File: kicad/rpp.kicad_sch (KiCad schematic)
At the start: 13 parts, among them J1 SolderPad, J2 SolderPad, J3 SolderPad, J4 SolderPad, Q1 CSD19537Q3, U1 LM5050-1

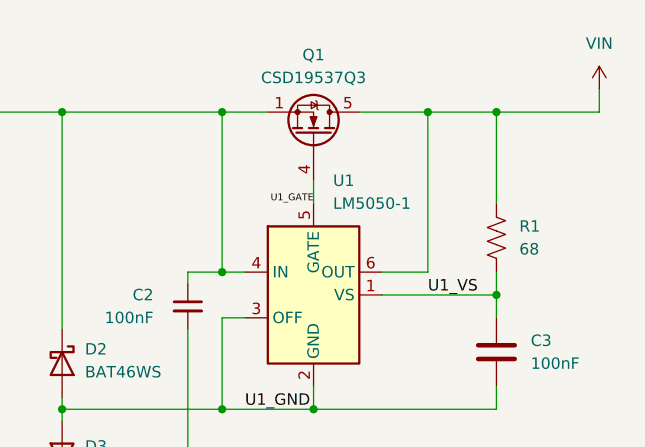
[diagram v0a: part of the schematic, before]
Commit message: Wrong design files initially commited
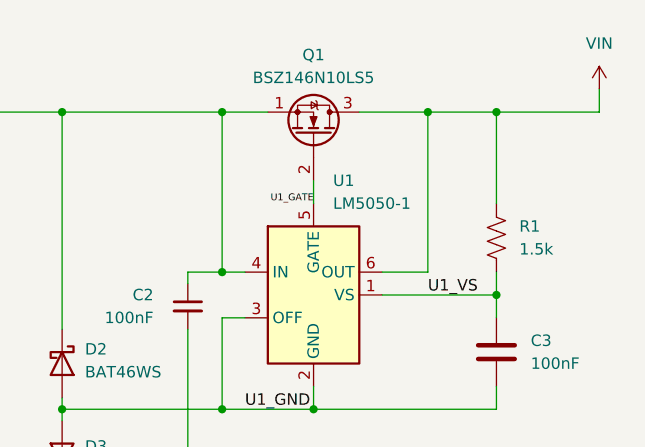
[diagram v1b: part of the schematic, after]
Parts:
- Q1: value CSD19537Q3 -> BSZ146N10LS5; footprint Package_SON_JJ:Texas_DQG0008A_3.3x3.3mm_P0.65mm_ThermalVias-D0.3mm -> Package_SON_JJ:Infineon_PG-TSDSON-8-26_3.3x3.3mm_P0.65mm_ThermalVias-D0.3mm; symbol Transistor_FET:CSD19537Q3 -> Julian_Symbols:BSZ096N10LS5; FT Rotation Offset 0 -> -90; LCSC PN C134143 -> C3289340; Manufacturer Texas Instruments -> Infineon Technologies; Part Number CSD19537Q3T -> BSZ146N10LS5ATMA1
- R1: value 68 -> 1.5k; LCSC PN C27592 -> C22843; Part Number 0603WAF680JT5E -> 0603WAF1501T5E; Part Type Preferred Extended -> Basic
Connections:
- net U1_GATE: now also Q1.2 (G); no longer Q1.4 (G)
- net VBAT: no longer Q1.2 (S), Q1.3 (S)
- net VIN: now also Q1.3 (D); no longer Q1.5 (D)
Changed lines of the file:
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@@
 	(title_block
 		(title "Super Step Down V3")
-		(date "2025-12-02")
+		(date "2026-02-06")
 		(rev "D")
 		(company "Author: Julian Joaquin")
 		(comment 1 "Licensed under CERN-OHL-W version 2")
-		(comment 2 "Copyright © Julian Joaquin, 2025")
+		(comment 2 "Copyright © Julian Joaquin, 2026")
 		(comment 4 "A 12S battery eliminator circuit (BEC) for UAS applications.")
 	)
@@
 		(dnp no)
 		(fields_autoplaced yes)
-		(property "Reference" "#PWR08"
+		(property "Reference" "#PWR04"
 			(at 130.81 88.9 0)
 			(effects
@@
 			(project "SSDV3"
 				(path "/ea689c3b-fea3-4fc0-9d65-1fb672b240d8/2c5420f9-cdfd-4ae0-879c-cf9dbf3cb514"
-					(reference "#PWR08")
+					(reference "#PWR04")
 					(unit 1)
 				)
@@
 		(dnp no)
 		(fields_autoplaced yes)
-		(property "Reference" "#PWR023"
+		(property "Reference" "#PWR06"
 			(at 172.72 168.91 0)
 			(effects
@@
 			(project "SSDV3"
 				(path "/ea689c3b-fea3-4fc0-9d65-1fb672b240d8/2c5420f9-cdfd-4ae0-879c-cf9dbf3cb514"
-					(reference "#PWR023")
+					(reference "#PWR06")
 					(unit 1)
 				)
@@
 		(on_board yes)
 		(dnp no)
-		(property "Reference" "#PWR09"
+		(property "Reference" "#PWR05"
 			(at 143.51 80.01 0)
 			(effects
@@
 			(project "SSDV3"
 				(path "/ea689c3b-fea3-4fc0-9d65-1fb672b240d8/2c5420f9-cdfd-4ae0-879c-cf9dbf3cb514"
-					(reference "#PWR09")
+					(reference "#PWR05")
 					(unit 1)
 				)
@@
 		(dnp no)
 		(fields_autoplaced yes)
-		(property "Reference" "#FLG06"
+		(property "Reference" "#FLG01"
 			(at 159.385 168.91 0)
 			(effects
@@
 			(project "SSDV3"
 				(path "/ea689c3b-fea3-4fc0-9d65-1fb672b240d8/2c5420f9-cdfd-4ae0-879c-cf9dbf3cb514"
-					(reference "#FLG06")
+					(reference "#FLG01")
 					(unit 1)
 				)
@@
 		(on_board yes)
 		(dnp no)
-		(property "Reference" "#PWR014"
+		(property "Reference" "#PWR09"
 			(at 215.9 130.81 0)
 			(effects
@@
 			(project "SSDV3"
 				(path "/ea689c3b-fea3-4fc0-9d65-1fb672b240d8/2c5420f9-cdfd-4ae0-879c-cf9dbf3cb514"
-					(reference "#PWR014")
+					(reference "#PWR09")
 					(unit 1)
 				)
@@
 		(on_board yes)
 		(dnp no)
-		(property "Reference" "#PWR018"
+		(property "Reference" "#PWR07"
 			(at 162.56 173.99 0)
 			(effects
@@
 			(project "SSDV3"
 				(path "/ea689c3b-fea3-4fc0-9d65-1fb672b240d8/2c5420f9-cdfd-4ae0-879c-cf9dbf3cb514"
-					(reference "#PWR018")
-					(unit 1)
-				)
-			)
-		)
-	)
-	(symbol
-		(lib_id "power:PWR_FLAG")
-		(at 161.29 179.07 90)
-		(unit 1)
-		(exclude_from_sim no)
-		(in_bom yes)
-		(on_board yes)
-		(dnp no)
-		(fields_autoplaced yes)
-		(property "Reference" "#FLG08"
-			(at 159.385 179.07 0)
-			(effects
-				(font
-					(size 1.27 1.27)
-				)
-				(hide yes)
-			)
-		)
-		(property "Value" "PWR_FLAG"
-			(at 157.48 179.07 90)
-			(effects
-				(font
-					(size 1.27 1.27)
-				)
-				(justify left)
-			)
-		)
-		(property "Footprint" ""
-			(at 161.29 179.07 0)
-			(effects
-				(font
-					(size 1.27 1.27)
-				)
-				(hide yes)
-			)
-		)
-		(property "Datasheet" "~"
-			(at 161.29 179.07 0)
-			(effects
-				(font
-					(size 1.27 1.27)
-				)
-				(hide yes)
-			)
-		)
-		(property "Description" "Special symbol for telling ERC where power comes from"
-			(at 161.29 179.07 0)
-			(effects
-				(font
-					(size 1.27 1.27)
-				)
-				(hide yes)
-			)
-		)
-		(pin "1"
-		)
-		(instances
-			(project "SSDV3"
-				(path "/ea689c3b-fea3-4fc0-9d65-1fb672b240d8/2c5420f9-cdfd-4ae0-879c-cf9dbf3cb514"
-					(reference "#FLG08")
+					(reference "#PWR07")
 					(unit 1)
 				)
@@
 			)
 		)
-		(property "Value" "68"
+		(property "Value" "1.5k"
 			(at 207.01 93.98 0)
 			(effects
@@
 			)
 		)
-		(property "Description" "RES 68Ω 1% 75V 100mW 0603"
+		(property "Description" "RES 1.5kΩ 1% 75V 100mW 0603"
 			(at 204.47 92.71 0)
 			(effects
@@
 			)
 		)
-		(property "LCSC PN" "C27592"
+		(property "LCSC PN" "C22843"
 			(at 204.47 92.71 0)
 			(effects
@@
 			)
 		)
-		(property "Part Type" "Preferred Extended"
+		(property "Part Type" "Basic"
 			(at 204.47 92.71 0)
 			(effects
@@
 			)
 		)
-		(property "Part Number" "0603WAF680JT5E"
+		(property "Part Number" "0603WAF1501T5E"
 			(at 204.47 92.71 0)
 			(effects
@@
 				(path "/ea689c3b-fea3-4fc0-9d65-1fb672b240d8/2c5420f9-cdfd-4ae0-879c-cf9dbf3cb514"
 					(reference "R1")
+					(unit 1)
+				)
+			)
+		)
+	)
+	(symbol
+		(lib_id "power:PWR_FLAG")
+		(at 161.29 179.07 90)
+		(unit 1)
+		(exclude_from_sim no)
+		(in_bom yes)
+		(on_board yes)
+		(dnp no)
+		(fields_autoplaced yes)
+		(property "Reference" "#FLG03"
+			(at 159.385 179.07 0)
+			(effects
+				(font
+					(size 1.27 1.27)
+				)
+				(hide yes)
+			)
+		)
+		(property "Value" "PWR_FLAG"
+			(at 157.48 179.07 90)
+			(effects
+				(font
+					(size 1.27 1.27)
+				)
+				(justify left)
+			)
+		)
+		(property "Footprint" ""
+			(at 161.29 179.07 0)
+			(effects
+				(font
+					(size 1.27 1.27)
+				)
+				(hide yes)
+			)
+		)
+		(property "Datasheet" "~"
+			(at 161.29 179.07 0)
+			(effects
+				(font
+					(size 1.27 1.27)
+				)
+				(hide yes)
+			)
+		)
+		(property "Description" "Special symbol for telling ERC where power comes from"
+			(at 161.29 179.07 0)
+			(effects
+				(font
+					(size 1.27 1.27)
+				)
+				(hide yes)
+			)
+		)
+		(pin "1"
+		)
+		(instances
+			(project "SSDV3"
+				(path "/ea689c3b-fea3-4fc0-9d65-1fb672b240d8/2c5420f9-cdfd-4ae0-879c-cf9dbf3cb514"
+					(reference "#FLG03")
 					(unit 1)
 				)
@@
 	)
 	(symbol
-		(lib_id "Transistor_FET:CSD19537Q3")
+		(lib_id "Julian_Symbols:BSZ096N10LS5")
 		(at 184.15 81.28 270)
 		(mirror x)
@@
 			)
 		)
-		(property "Value" "CSD19537Q3"
+		(property "Value" "BSZ146N10LS5"
 			(at 184.15 74.93 90)
 			(effects
@@
 			)
 		)
-		(property "Footprint" "Package_SON_JJ:Texas_DQG0008A_3.3x3.3mm_P0.65mm_ThermalVias-D0.3mm"
+		(property "Footprint" "Package_SON_JJ:Infineon_PG-TSDSON-8-26_3.3x3.3mm_P0.65mm_ThermalVias-D0.3mm"
 			(at 182.245 76.2 0)
 			(effects
@@
 			)
 		)
-		(property "Datasheet" "http://www.ti.com/lit/ds/symlink/csd19537q3.pdf"
+		(property "Datasheet" "https://www.infineon.com/assets/row/public/documents/24/49/infineon-bsz146n10ls5-datasheet-en.pdf"
 			(at 180.34 76.2 0)
 			(effects
@@
 			)
 		)
-		(property "Description" "MOSFET N-CH 100V 53A VSON-8(3.3x3.3)"
+		(property "Description" "MOSFET N-CH 100V 44A TSDSON-8FL"
 			(at 184.15 81.28 0)
 			(effects
@@
 			)
 		)
-		(property "LCSC PN" "C134143"
+		(property "LCSC PN" "C3289340"
 			(at 184.15 81.28 90)
 			(effects
@@
 			)
 		)
-		(property "Manufacturer" "Texas Instruments"
+		(property "Manufacturer" "Infineon Technologies"
 			(at 184.15 81.28 90)
 			(effects
@@
 			)
 		)
-		(property "Part Number" "CSD19537Q3T"
+		(property "Part Number" "BSZ146N10LS5ATMA1"
 			(at 184.15 81.28 90)
 			(effects
@@
 			)
 		)
-		(property "FT Rotation Offset" "0"
+		(property "FT Rotation Offset" "-90"
 			(at 184.15 81.28 90)
 			(effects
@@
 			)
 		)
-		(pin "5"
-		)
 		(pin "2"
 		)
@@
 		)
 		(pin "1"
-		)
-		(pin "4"
 		)
 		(instances
@@
 		(dnp no)
 		(fields_autoplaced yes)
-		(property "Reference" "#PWR013"
+		(property "Reference" "#PWR08"
 			(at 215.9 80.01 0)
 			(effects
@@
 			(project "SSDV3"
 				(path "/ea689c3b-fea3-4fc0-9d65-1fb672b240d8/2c5420f9-cdfd-4ae0-879c-cf9dbf3cb514"
-					(reference "#PWR013")
+					(reference "#PWR08")
 					(unit 1)
 				)

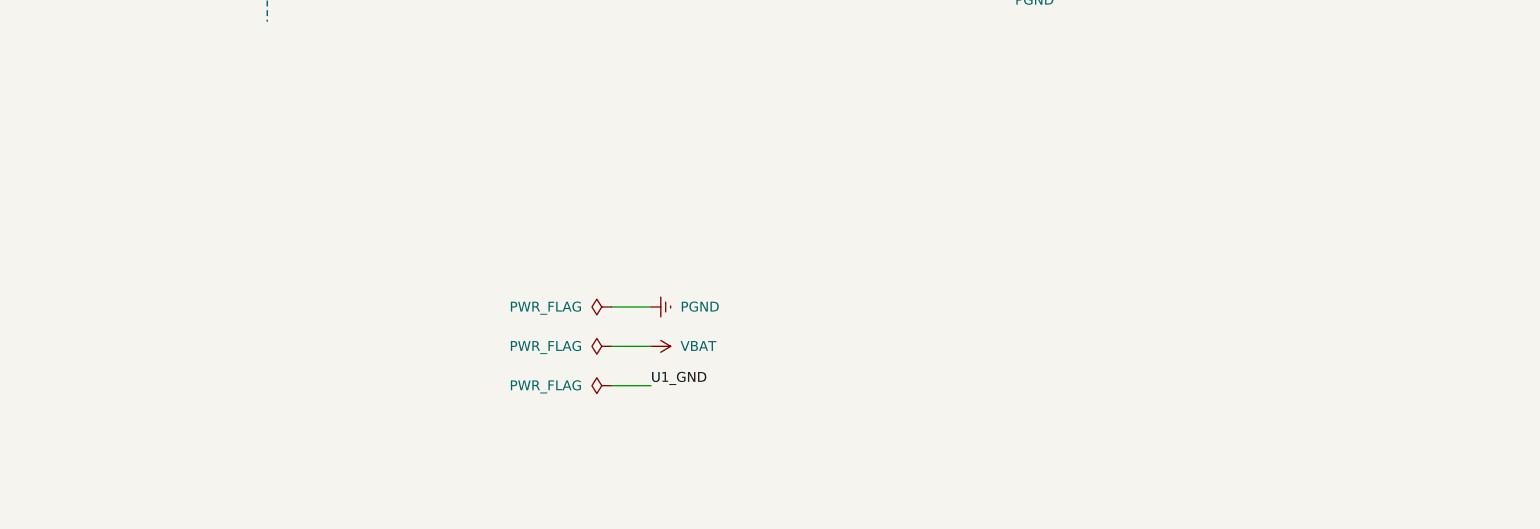
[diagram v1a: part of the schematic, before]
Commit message: Added UBCO trademark notice, prepared for production
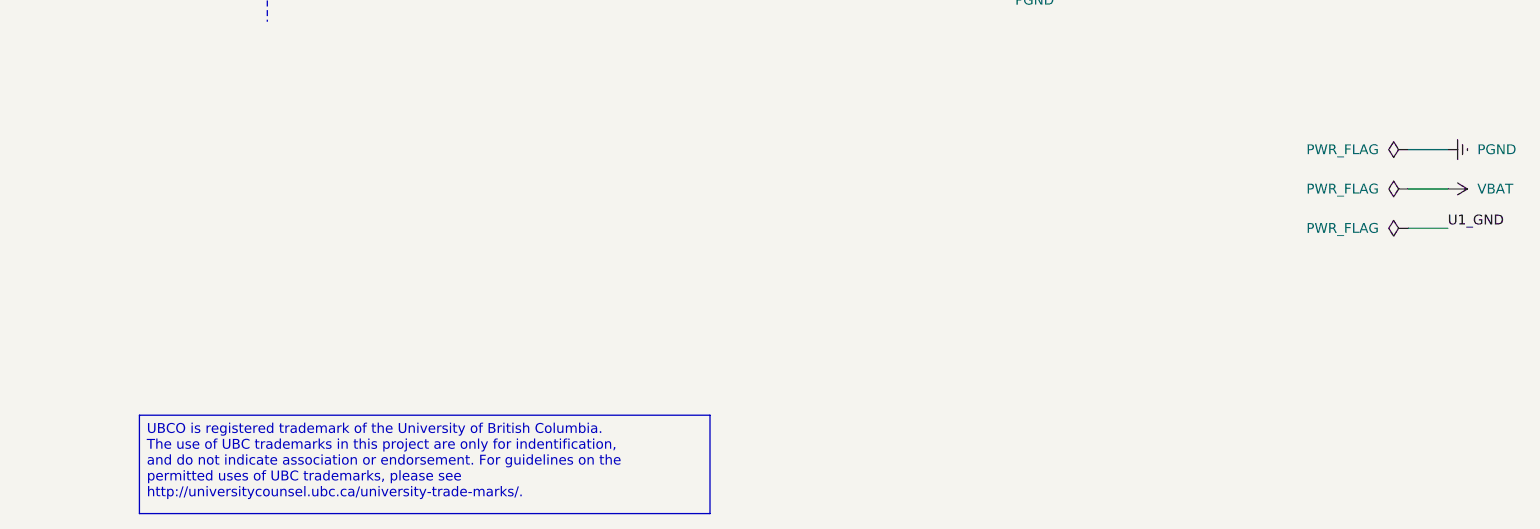
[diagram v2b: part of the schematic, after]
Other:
- company: Author: Julian Joaquin -> UBCO Aerospace
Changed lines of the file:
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@@
 		(date "2026-02-06")
 		(rev "D")
-		(company "Author: Julian Joaquin")
+		(company "UBCO Aerospace")
 		(comment 1 "Licensed under CERN-OHL-W version 2")
 		(comment 2 "Copyright © Julian Joaquin, 2026")
@@
 		)
 	)
+	(text_box "UBCO is registered trademark of the University of British Columbia.\nThe use of UBC trademarks in this project are only for indentification,\nand do not indicate association or endorsement. For guidelines on the\npermitted uses of UBC trademarks, please see\nhttp://universitycounsel.ubc.ca/university-trade-marks/."
+		(exclude_from_sim no)
+		(at 100.33 182.88 0)
+		(size 73.66 12.7)
+		(margins 0.9525 0.9525 0.9525 0.9525)
+		(stroke
+			(width 0)
+			(type solid)
+			(color 132 0 0 1)
+		)
+		(fill
+			(type none)
+		)
+		(effects
+			(font
+				(size 1.27 1.27)
+				(color 132 0 0 1)
+			)
+			(justify left top)
+			(href "http://universitycounsel.ubc.ca/university-trade-marks")
+		)
+	)
 	(junction
 		(at 173.99 78.74)
@@
 	(wire
 		(pts
-			(xy 161.29 179.07) (xy 166.37 179.07)
+			(xy 264.16 158.75) (xy 269.24 158.75)
 		)
 		(stroke
@@
 	(wire
 		(pts
-			(xy 161.29 168.91) (xy 166.37 168.91)
+			(xy 264.16 148.59) (xy 269.24 148.59)
 		)
 		(stroke
@@
 	(wire
 		(pts
-			(xy 161.29 173.99) (xy 166.37 173.99)
+			(xy 264.16 153.67) (xy 269.24 153.67)
 		)
 		(stroke
@@
 	)
 	(label "U1_GND"
-		(at 166.37 179.07 0)
+		(at 269.24 158.75 0)
 		(effects
 			(font
@@
 	(symbol
 		(lib_id "power:Earth")
-		(at 166.37 168.91 90)
+		(at 269.24 148.59 90)
 		(unit 1)
 		(exclude_from_sim no)
@@
 		(fields_autoplaced yes)
 		(property "Reference" "#PWR06"
-			(at 172.72 168.91 0)
+			(at 275.59 148.59 0)
 			(effects
 				(font
@@
 		)
 		(property "Value" "PGND"
-			(at 170.18 168.91 90)
+			(at 273.05 148.59 90)
 			(effects
 				(font
@@
 		)
 		(property "Footprint" ""
-			(at 166.37 168.91 0)
+			(at 269.24 148.59 0)
 			(effects
 				(font
@@
 		)
 		(property "Datasheet" "~"
-			(at 166.37 168.91 0)
+			(at 269.24 148.59 0)
 			(effects
 				(font
@@
 		)
 		(property "Description" "Power symbol creates a global label with name \"Earth\""
-			(at 166.37 168.91 0)
+			(at 269.24 148.59 0)
 			(effects
 				(font
@@
 	(symbol
 		(lib_id "power:PWR_FLAG")
-		(at 161.29 173.99 90)
+		(at 264.16 153.67 90)
 		(unit 1)
 		(exclude_from_sim no)
@@
 		(fields_autoplaced yes)
 		(property "Reference" "#FLG02"
-			(at 159.385 173.99 0)
+			(at 262.255 153.67 0)
 			(effects
 				(font
@@
 		)
 		(property "Value" "PWR_FLAG"
-			(at 157.48 173.99 90)
+			(at 260.35 153.67 90)
 			(effects
 				(font
@@
 		)
 		(property "Footprint" ""
-			(at 161.29 173.99 0)
+			(at 264.16 153.67 0)
 			(effects
 				(font
@@
 		)
 		(property "Datasheet" "~"
-			(at 161.29 173.99 0)
+			(at 264.16 153.67 0)
 			(effects
 				(font
@@
 		)
 		(property "Description" "Special symbol for telling ERC where power comes from"
-			(at 161.29 173.99 0)
+			(at 264.16 153.67 0)
 			(effects
 				(font
@@
 	(symbol
 		(lib_id "power:PWR_FLAG")
-		(at 161.29 168.91 90)
+		(at 264.16 148.59 90)
 		(unit 1)
 		(exclude_from_sim no)
@@
 		(fields_autoplaced yes)
 		(property "Reference" "#FLG01"
-			(at 159.385 168.91 0)
+			(at 262.255 148.59 0)
 			(effects
 				(font
@@
 		)
 		(property "Value" "PWR_FLAG"
-			(at 157.48 168.91 90)
+			(at 260.35 148.59 90)
 			(effects
 				(font
@@
 		)
 		(property "Footprint" ""
-			(at 161.29 168.91 0)
+			(at 264.16 148.59 0)
 			(effects
 				(font
@@
 		)
 		(property "Datasheet" "~"
-			(at 161.29 168.91 0)
+			(at 264.16 148.59 0)
 			(effects
 				(font
@@
 		)
 		(property "Description" "Special symbol for telling ERC where power comes from"
-			(at 161.29 168.91 0)
+			(at 264.16 148.59 0)
 			(effects
 				(font
@@
 	(symbol
 		(lib_id "power:VDDA")
-		(at 166.37 173.99 270)
+		(at 269.24 153.67 270)
 		(unit 1)
 		(exclude_from_sim no)
@@
 		(dnp no)
 		(property "Reference" "#PWR07"
-			(at 162.56 173.99 0)
+			(at 265.43 153.67 0)
 			(effects
 				(font
@@
 		)
 		(property "Value" "VBAT"
-			(at 170.18 173.99 90)
+			(at 273.05 153.67 90)
 			(effects
 				(font
@@
 		)
 		(property "Footprint" ""
-			(at 166.37 173.99 0)
+			(at 269.24 153.67 0)
 			(effects
 				(font
@@
 		)
 		(property "Datasheet" ""
-			(at 166.37 173.99 0)
+			(at 269.24 153.67 0)
 			(effects
 				(font
@@
 		)
 		(property "Description" "Power symbol creates a global label with name \"VDDA\""
-			(at 166.37 173.99 0)
+			(at 269.24 153.67 0)
 			(effects
 				(font
@@
 	(symbol
 		(lib_id "power:PWR_FLAG")
-		(at 161.29 179.07 90)
+		(at 264.16 158.75 90)
 		(unit 1)
 		(exclude_from_sim no)
@@
 		(fields_autoplaced yes)
 		(property "Reference" "#FLG03"
-			(at 159.385 179.07 0)
+			(at 262.255 158.75 0)
 			(effects
 				(font
@@
 		)
 		(property "Value" "PWR_FLAG"
-			(at 157.48 179.07 90)
+			(at 260.35 158.75 90)
 			(effects
 				(font
@@
 		)
 		(property "Footprint" ""
-			(at 161.29 179.07 0)
+			(at 264.16 158.75 0)
 			(effects
 				(font
@@
 		)
 		(property "Datasheet" "~"
-			(at 161.29 179.07 0)
+			(at 264.16 158.75 0)
 			(effects
 				(font
@@
 		)
 		(property "Description" "Special symbol for telling ERC where power comes from"
-			(at 161.29 179.07 0)
-			(effects
-				(font
+			(at 264.16 158.75 0)
+			(effects
+				(font
